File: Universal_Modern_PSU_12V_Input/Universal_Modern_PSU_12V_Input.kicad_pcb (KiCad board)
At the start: 2 copper layers, 70 x 50 mm, 24 parts, among them J1 +12VDC Input, J2 Power Output, Q1 SUP53P06-20-E3, U1 DFR0831, U2 NKE1212SC, U3 R-78CK5.0-0.5

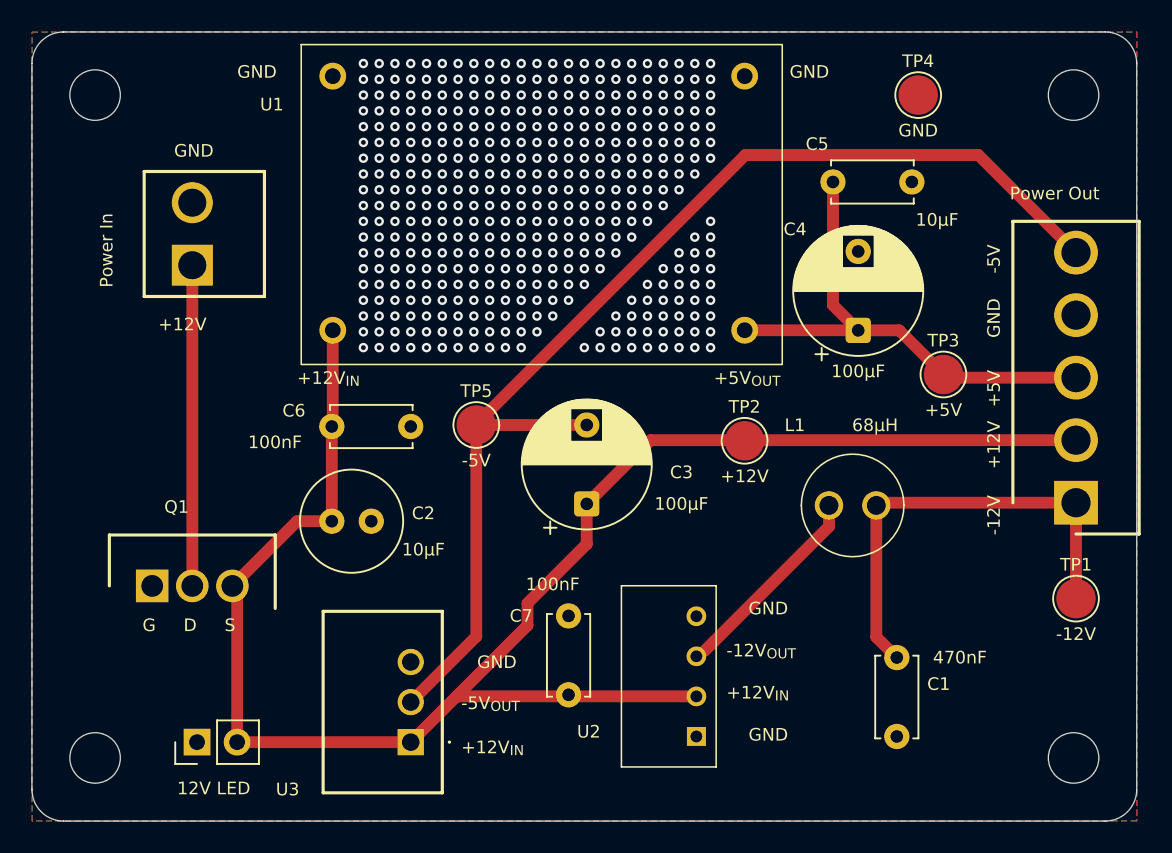
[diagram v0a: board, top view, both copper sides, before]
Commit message: Thickened +5V & +12V tracks
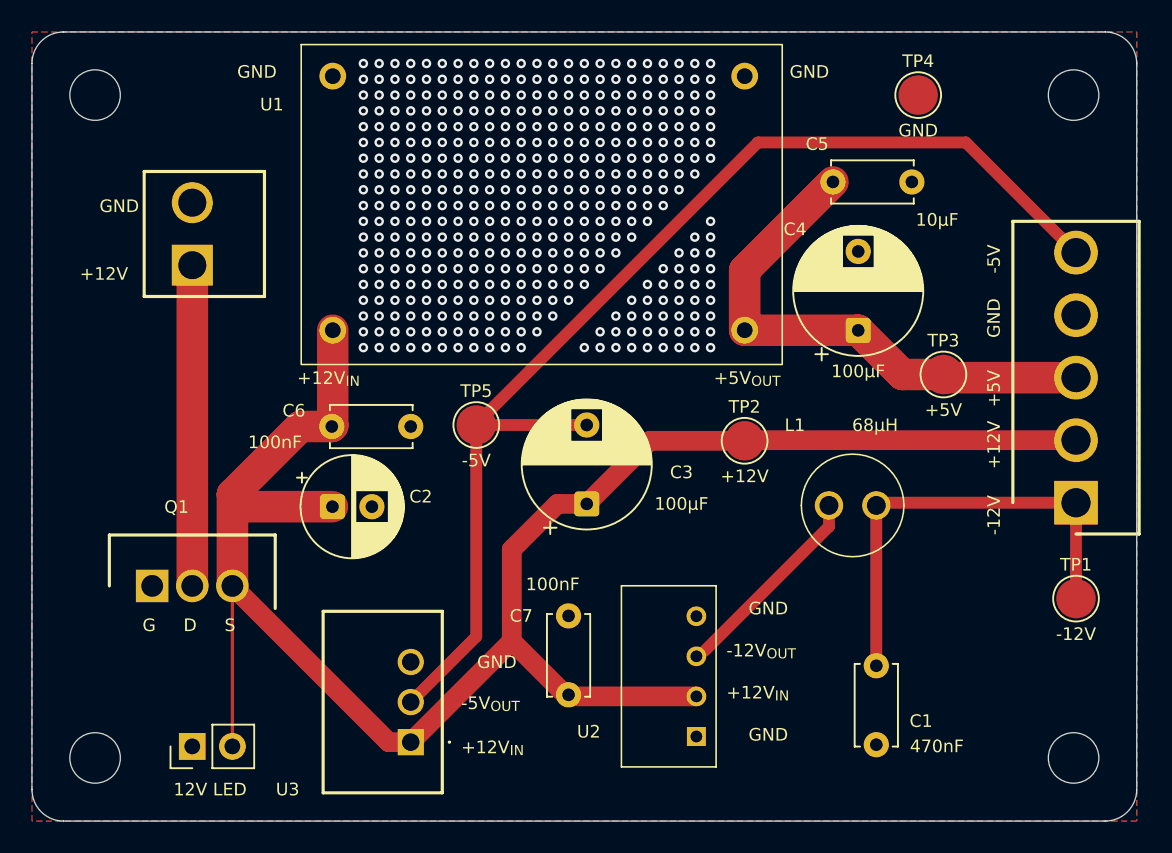
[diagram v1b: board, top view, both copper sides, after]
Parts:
- C2: footprint Capacitor_THT:C_Radial_D6.3mm_H7.0mm_P2.50mm -> Capacitor_THT:CP_Radial_D6.3mm_P2.50mm
- moved C1 1.40 mm to (159.5, 123.6)
- moved C2 0.92 mm to (125.1, 108.6)
- moved D1 0.40 mm to (116.2, 123.7)
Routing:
- net /+12V_{OUT}: track 109.2 -> 119.9 mm
- net /+5V_{OUT}: track 32.3 -> 34.0 mm
- net /-5V_{OUT}: track 74.0 -> 74.6 mm
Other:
- board text removed: "Power In"
- board text removed: "Power Out"

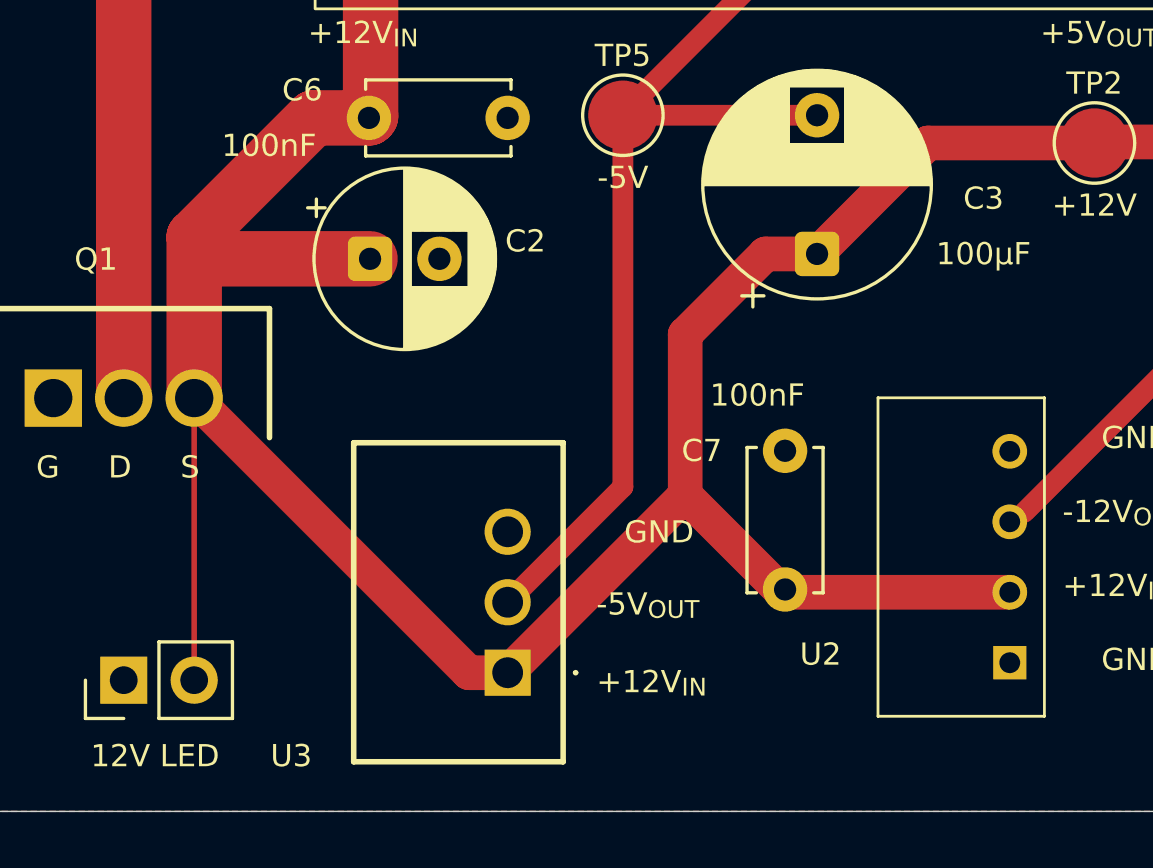
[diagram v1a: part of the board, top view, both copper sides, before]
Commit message: Additional vias for heat conduction
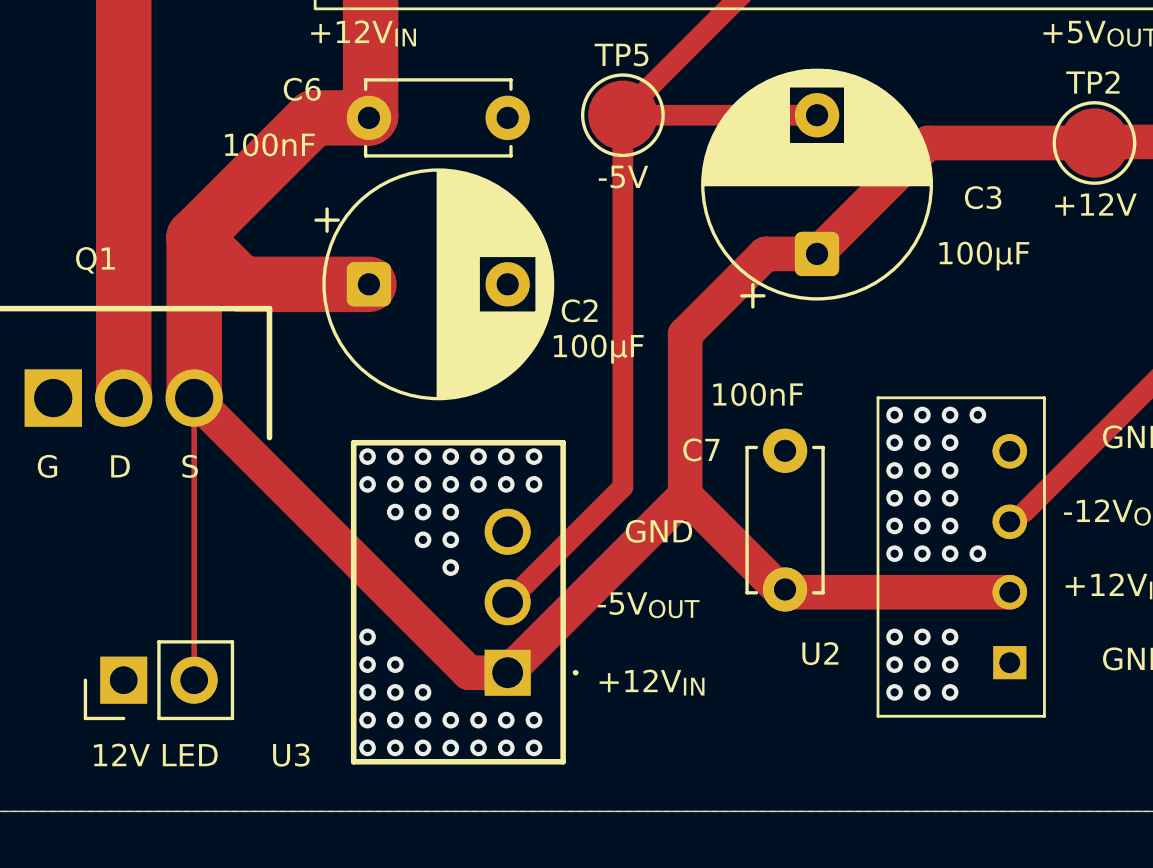
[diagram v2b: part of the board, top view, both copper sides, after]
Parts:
- C2: value 10µF -> 100µF; footprint Capacitor_THT:CP_Radial_D6.3mm_P2.50mm -> Capacitor_THT:CP_Radial_D8.0mm_P5.00mm
- moved C2 0.92 mm to (125.0, 109.5)
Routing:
- net /GND: vias 404 -> 473
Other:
- board text added: "Universal Vintage Computer Power Supply (Rev A) Brett Hallen, Nov 2025 www.youtube.com/@Brfff"
- board text removed: "Universal Vintage Computer Power Supply (Rev A) Brett Hallen, Nov 2025 www.youtube.com/@Brff"

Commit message: Minor PCB & schematic changes
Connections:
- C2 pad 1: /+12V_{OUT} -> /+12V_{IN}
- C3 pad 1: /+12V_{OUT} -> /+12V_{IN}
- C6 pad 1: /+12V_{OUT} -> /+12V_{IN}
- C7 pad 2: /+12V_{OUT} -> /+12V_{IN}
- D1 pad 2: /+12V_{OUT} -> /+12V_{IN}
- J1 pad 1: /+12V_{IN} -> /+12V_{SUPPLY}
- J2 pad 2: /+12V_{OUT} -> /+12V_{IN}
- Q1 pad 2: /+12V_{IN} -> /+12V_{SUPPLY}
- Q1 pad 3: /+12V_{OUT} -> /+12V_{IN}
- TP2 pad 1: /+12V_{OUT} -> /+12V_{IN}
- U1 pad 2: /+12V_{OUT} -> /+12V_{IN}
- U2 pad 2: /+12V_{OUT} -> /+12V_{IN}
- U3 pad 1: /+12V_{OUT} -> /+12V_{IN}
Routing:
- net /+12V_{OUT}: track 120.3 -> 0.00 mm
- net /+12V_{IN}: track 20.3 -> 120.3 mm
- net /+12V_{SUPPLY}: track 0.00 -> 20.3 mm
- net /-5V_{OUT}: track 74.6 -> 61.8 mm
- net /GND: vias 473 -> 506

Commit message: Further refinements to PCB layout
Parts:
- moved TP1 12.7 mm to (161.1, 108.3)
- moved C1 11.5 mm to (164.6, 113.3)
- moved C4 8.63 mm to (156.0, 89.1)
- moved C5 8.39 mm to (158.5, 95.7)
- moved TP3 7.82 mm to (163.2, 92.4)
- moved L1 4.79 mm to (156.0, 111.7)
- moved TP5 4.32 mm to (134.0, 107.7)
- moved J1 2.83 mm to (113.6, 94.4)
- moved Q1 2.58 mm to (111.1, 113.4)
- moved C2 2.58 mm to (122.6, 108.8)
- moved C6 2.58 mm to (122.6, 102.8)
- moved U1 2.57 mm to (134.0, 77.9)
- moved C7 1.67 mm to (139.7, 117.1)
- moved U2 1.66 mm to (147.8, 124.8)
- moved C3 1.33 mm to (141.0, 109.7)
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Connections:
- J2 pad 3: /+5V_{OUT} -> /-5V_{OUT}
- J2 pad 5: /-5V_{OUT} -> /+5V_{OUT}
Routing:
- net /-12V_{OUT}: track 29.0 -> 17.6 mm
- net /-5V_{OUT}: track 61.8 -> 56.1 mm
- net /+5V_{OUT}: track 34.0 -> 30.9 mm
- net /-12V: track 12.5 -> 10.1 mm
- net /+12V_{IN}: track 120.3 -> 118.3 mm
- net /+12V_{SUPPLY}: track 20.3 -> 19.0 mm
- net /GND: vias 506 -> 513
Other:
- board text added: "GND +12V"

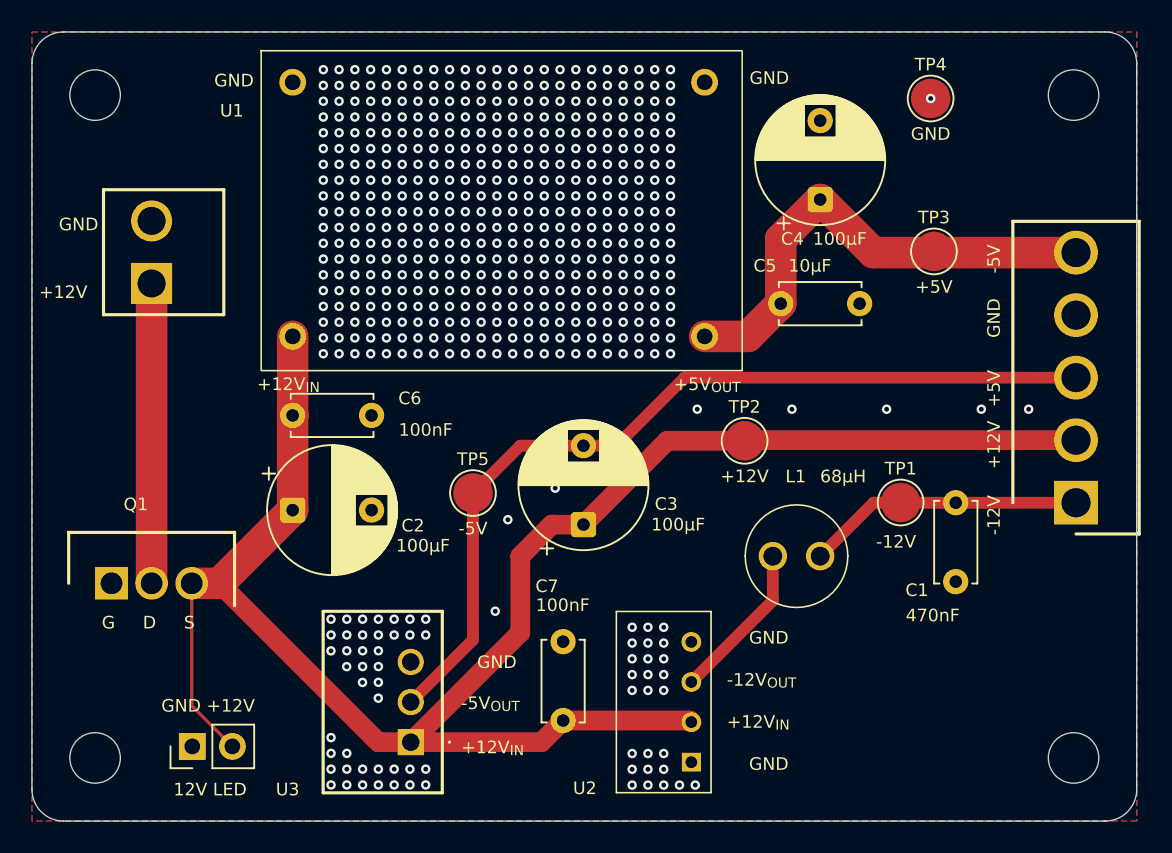
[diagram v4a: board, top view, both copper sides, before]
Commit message: Implement schematic changes to PCB
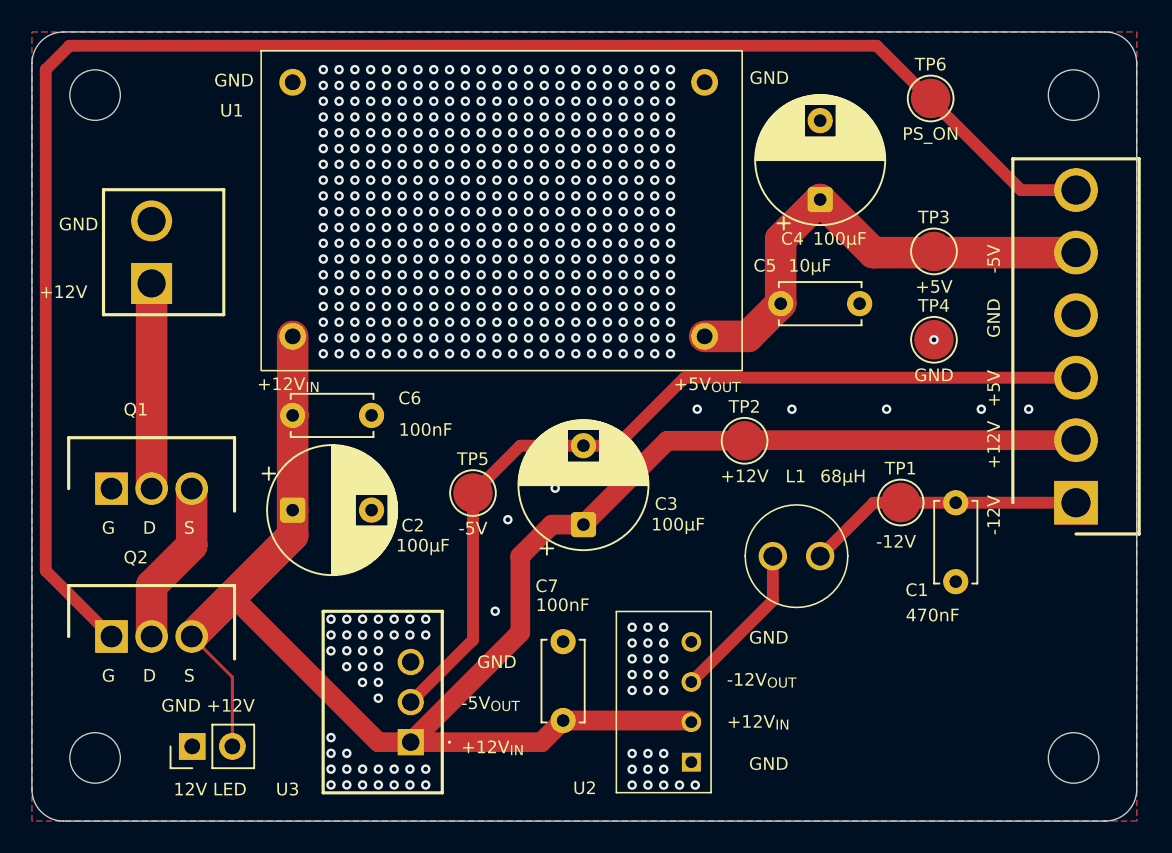
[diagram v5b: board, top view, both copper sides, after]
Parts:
- added Q2: SUP53P06-20-E3, Clueless_Engineer:TO254P465X1028X1931-3P, F.Cu at (111.1, 116.8)
- added TP6: PS_ON, TestPoint:TestPoint_Pad_D2.5mm, F.Cu at (163.0, 82.7)
- J2: footprint Clueless_Engineer:640445-5 -> Clueless_Engineer:640445-6
- moved TP4 15.3 mm to (163.2, 98.0)
- moved Q1 6.00 mm to (111.1, 107.4)
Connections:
- Q1 pad 3: /+12V_{IN} -> Net-(Q1-S)
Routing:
- net /PS_ON_{IN}: track 0.00 -> 107.3 mm
- net Net-(Q1-S): track 0.00 -> 10.4 mm
- net /+12V_{SUPPLY}: track 19.0 -> 13.0 mm
- net /+12V_{IN}: track 118.3 -> 116.1 mm
